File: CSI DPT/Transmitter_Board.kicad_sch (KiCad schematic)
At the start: 5 parts, among them J3 691137710002, U6 SN75451BDR

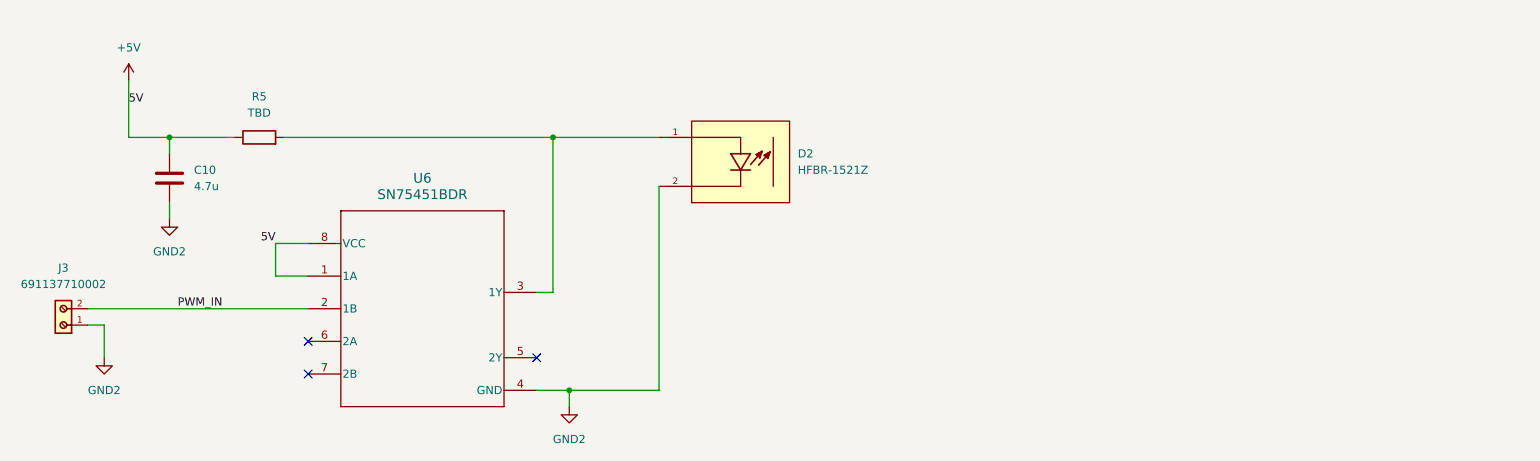
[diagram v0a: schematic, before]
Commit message: Nov.17 Update
Changed from opto PWM transmission to differential transmission. With added test point.
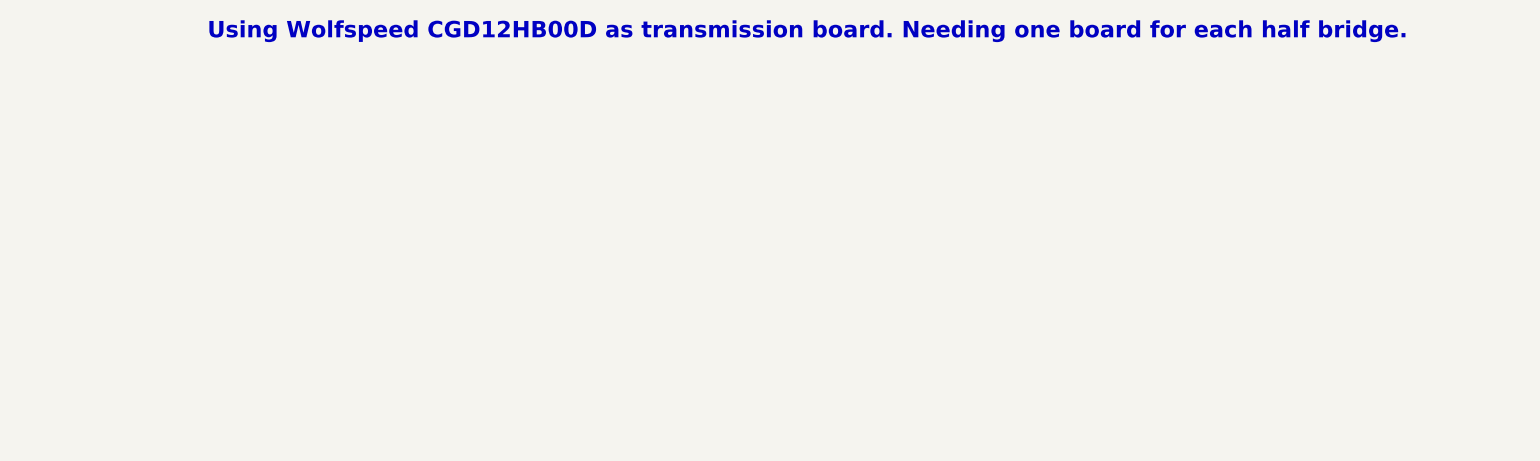
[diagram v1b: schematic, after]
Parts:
- removed C10: 4.7u, symbol Device:C
- removed D2: HFBR-1521Z, HFBR-1521Z:OPTO_HFBR-1521Z, symbol Opto_transmitter:HFBR-1521Z
- removed J3: 691137710002, VSI_DPT:691137710002, symbol VSI_DPT:691137710002
- removed R5: TBD, Resistor_SMD:R_1206_3216Metric, symbol Device:R_1206
- removed U6: SN75451BDR, D0008A_N, symbol SN75451BDR:SN75451BDR
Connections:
- no-connect marks 3 -> 0
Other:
- note added: "Using Wolfspeed CGD12HB00D as transmission board. Needing one board for each half bridge."
